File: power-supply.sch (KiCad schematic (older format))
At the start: 107 parts, among them IC1 TPS54561, J12 S2B-PH-K-S_LF__SN_, Q1 BSS138APW, Q2 BSS138APW, Q3 BSS138APW, Q4 BSS138APW, Q5 BSS138APW, Q6 BSS138APW, U10 TPS62823DLCT, U11 TPS62823DLCT, U12 TPS62823DLCT, U13 TPS62823DLCT, U16 TPS62823DLCT, U9 LM3881MME_NOPB

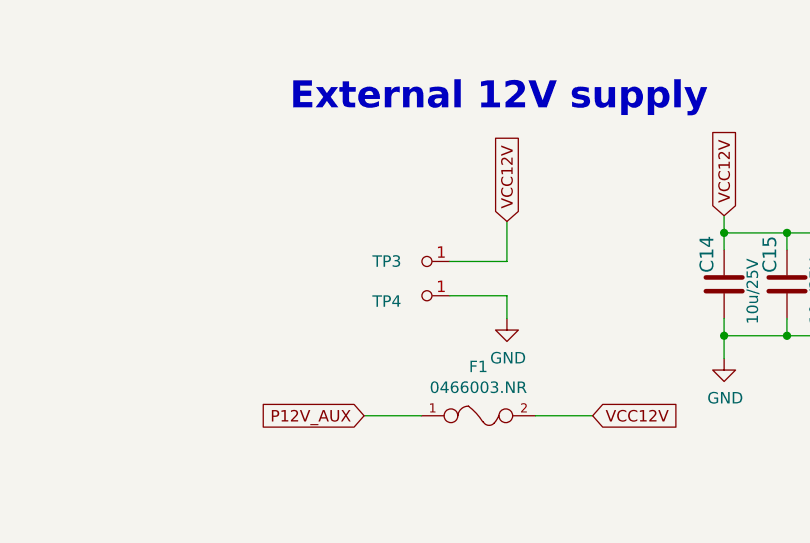
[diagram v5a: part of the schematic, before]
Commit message: Add aux pwr connector
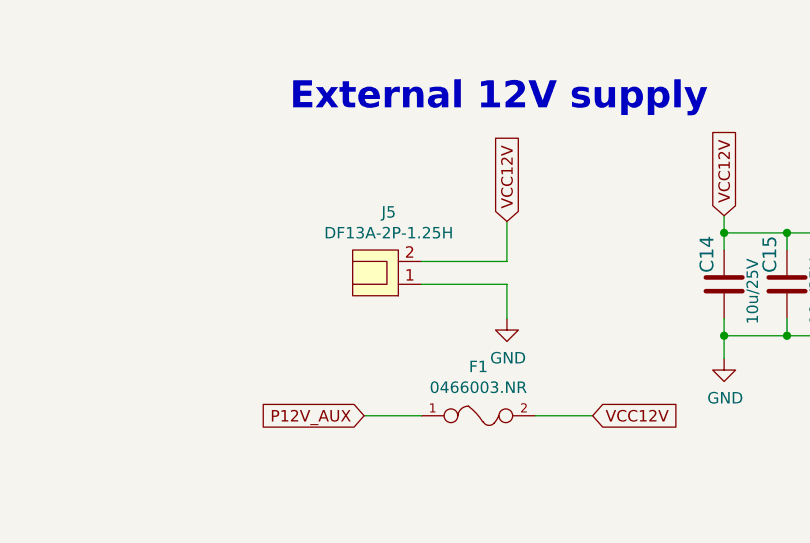
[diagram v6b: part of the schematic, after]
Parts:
- removed TP3, TP4: RCW-0C, artix-dc-scm-footprints:PROBE_PAD_1206, symbol artix-dc-scm:RCW-0C
- added J5: DF13A-2P-1.25H, artix-dc-scm-footprints:DF13A-2P-1.25H, symbol artix-dc-scm:DF13A-2P-1.25H
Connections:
- net GND: now also J5.1
- net VCC12V: now also J5.2
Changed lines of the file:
@@
-	0    1    1    0
-$EndComp
-$Comp
-L artix-dc-scm:RCW-0C TP3
-U 1 1 5FE83A9D
-P 1900 1575
-F 0 "TP3" V 1900 1400 50  0000 C CNN
-F 1 "RCW-0C" V 1766 1622 50  0001 C CNN
-F 2 "artix-dc-scm-footprints:PROBE_PAD_1206" H 2100 1775 60  0001 L CNN
-F 3 "https://www.te.com/commerce/DocumentDelivery/DDEController?Action=srchrtrv&DocNm=1773266&DocType=DS&DocLang=English" H 2100 1875 60  0001 L CNN
-F 4 "RCW-0C" H 2100 2075 60  0001 L CNN "MPN"
-F 5 "TE Connectivity AMP Connectors" H 2100 2675 60  0001 L CNN "Manufacturer"
-	1    1900 1575
-	0    1    1    0
-$EndComp
-$Comp
-L artix-dc-scm:RCW-0C TP4
-U 1 1 5FEA4BA8
-P 1900 1725
-F 0 "TP4" V 1925 1550 50  0000 C CNN
-F 1 "RCW-0C" V 1766 1772 50  0001 C CNN
-F 2 "artix-dc-scm-footprints:PROBE_PAD_1206" H 2100 1925 60  0001 L CNN
-F 3 "https://www.te.com/commerce/DocumentDelivery/DDEController?Action=srchrtrv&DocNm=1773266&DocType=DS&DocLang=English" H 2100 2025 60  0001 L CNN
-F 4 "RCW-0C" H 2100 2225 60  0001 L CNN "MPN"
-F 5 "TE Connectivity AMP Connectors" H 2100 2825 60  0001 L CNN "Manufacturer"
-	1    1900 1725
 	0    1    1    0
 $EndComp
 Text GLabel 2250 1400 1    50   Input ~ 0
 VCC12V
-Wire Wire Line
-	2000 1575 2250 1575
 Wire Wire Line
 	2250 1575 2250 1400
@@
 $EndComp
 Wire Wire Line
-	2000 1725 2250 1725
-Wire Wire Line
-	2250 1725 2250 1825
+	2250 1675 2250 1825
 Text GLabel 1625 2250 0    50   Input ~ 0
 P12V_AUX
@@
 Text Notes 8825 5925 0    50   ~ 0
 3v3 required by I3C translator
+$Comp
+L artix-dc-scm:DF13A-2P-1.25H J5
+U 1 1 601AA6B2
+P 1675 1525
+F 0 "J5" H 1617 1360 50  0000 C CNN
+F 1 "DF13A-2P-1.25H" H 1617 1451 50  0000 C CNN
+F 2 "artix-dc-scm-footprints:DF13A-2P-1.25H" H 1575 1075 50  0001 C CNN
+F 3 "" H 1675 1475 50  0001 C CNN
+F 4 "DF13A-2P-1.25H" H 1725 1275 50  0001 C CNN "MPN"
+F 5 "Hirose" H 1675 1175 50  0001 C CNN "Manufacturer"
+	1    1675 1525
+	-1   0    0    1
+$EndComp
+Wire Wire Line
+	1875 1575 2250 1575
+Wire Wire Line
+	1875 1675 2250 1675
 $EndSCHEMATC

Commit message: Fix USB3300 circuit
-remove 1V8 connection
-add capacitance at internal 1v8 regulators
-apply changes to PCB
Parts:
- C101, C103, C2, C75, C76, C77, C78, C83, C84, C85, C86, C87, C88, C89, C90: footprint artix-dc-scm-footprints:0402-cap -> _autosave-artix-dc-scm-footprints:0402-cap; symbol artix-dc-scm:C_10u_0402 -> _autosave-artix-dc-scm:C_10u_0402
- C14, C15, C16: footprint artix-dc-scm-footprints:0603-cap -> _autosave-artix-dc-scm-footprints:0603-cap; symbol artix-dc-scm:C_10u_25V_0603 -> _autosave-artix-dc-scm:C_10u_25V_0603
- C3, C79, C80, C81, C82: footprint artix-dc-scm-footprints:0402-res -> _autosave-artix-dc-scm-footprints:0402-res; symbol artix-dc-scm:C_120p_0402 -> _autosave-artix-dc-scm:C_120p_0402
- C64, C69: footprint artix-dc-scm-footprints:0402-cap -> _autosave-artix-dc-scm-footprints:0402-cap; symbol artix-dc-scm:C_10n_0402 -> _autosave-artix-dc-scm:C_10n_0402
- C65, C66, C67: footprint artix-dc-scm-footprints:0603-cap -> _autosave-artix-dc-scm-footprints:0603-cap; symbol artix-dc-scm:C_2u2_0603_25V -> _autosave-artix-dc-scm:C_2u2_0603_25V
- C68: footprint artix-dc-scm-footprints:0402-cap -> _autosave-artix-dc-scm-footprints:0402-cap; symbol artix-dc-scm:C_4n7_0402 -> _autosave-artix-dc-scm:C_4n7_0402
- C70: footprint artix-dc-scm-footprints:0402-cap -> _autosave-artix-dc-scm-footprints:0402-cap; symbol artix-dc-scm:C_47p_0402 -> _autosave-artix-dc-scm:C_47p_0402
- C71: footprint artix-dc-scm-footprints:0402-cap -> _autosave-artix-dc-scm-footprints:0402-cap; symbol artix-dc-scm:C_100n_0402-artix-dc-scm -> _autosave-artix-dc-scm:C_100n_0402-artix-dc-scm
- C72, C73, C74: footprint artix-dc-scm-footprints:0603-cap -> _autosave-artix-dc-scm-footprints:0603-cap; symbol artix-dc-scm:C_47u_0603 -> _autosave-artix-dc-scm:C_47u_0603
- D14, D4, D5, D6, D7, D8: footprint artix-dc-scm-footprints:LED_0603 -> _autosave-artix-dc-scm-footprints:LED_0603; symbol artix-dc-scm:LG_L29K-G2J1-24-Z -> _autosave-artix-dc-scm:LG_L29K-G2J1-24-Z
- D3: footprint artix-dc-scm-footprints:PDS760-13 -> _autosave-artix-dc-scm-footprints:PDS760-13; symbol artix-dc-scm:PDS760-13 -> _autosave-artix-dc-scm:PDS760-13
- F1: footprint artix-dc-scm-footprints:1206-Fuse-Littelfuse-0466-0-0-MFG -> _autosave-artix-dc-scm-footprints:1206-Fuse-Littelfuse-0466-0-0-MFG; symbol artix-dc-scm:0466003.NR -> _autosave-artix-dc-scm:0466003.NR
- IC1: footprint artix-dc-scm-footprints:WSON-10_4x4 -> _autosave-artix-dc-scm-footprints:WSON-10_4x4; symbol artix-dc-scm:TPS54561 -> _autosave-artix-dc-scm:TPS54561
- J12: footprint artix-dc-scm-footprints:PinHeader_1x2_P2mm_Drill1mm_RA -> _autosave-artix-dc-scm-footprints:PinHeader_1x2_P2mm_Drill1mm_RA; symbol artix-dc-scm:S2B-PH-K-S_LF__SN_ -> _autosave-artix-dc-scm:S2B-PH-K-S_LF__SN_
- J5: footprint artix-dc-scm-footprints:DF13A-2P-1.25H -> _autosave-artix-dc-scm-footprints:DF13A-2P-1.25H; symbol artix-dc-scm:DF13A-2P-1.25H -> _autosave-artix-dc-scm:DF13A-2P-1.25H
- L1: footprint artix-dc-scm-footprints:WE_7447798720 -> _autosave-artix-dc-scm-footprints:WE_7447798720; symbol artix-dc-scm:WE_7447798720 -> _autosave-artix-dc-scm:WE_7447798720
- L2, L3, L4, L5, L6: footprint artix-dc-scm-footprints:IHLP-1212AE -> _autosave-artix-dc-scm-footprints:IHLP-1212AE; symbol artix-dc-scm:IHLP1212AEERR47M11 -> _autosave-artix-dc-scm:IHLP1212AEERR47M11
- Q1, Q2, Q3, Q4, Q5, Q6: footprint artix-dc-scm-footprints:SC70-3 -> _autosave-artix-dc-scm-footprints:SC70-3; symbol artix-dc-scm:BSS138APW -> _autosave-artix-dc-scm:BSS138APW
- R138, R14, R15, R16, R185: footprint artix-dc-scm-footprints:0402-res -> _autosave-artix-dc-scm-footprints:0402-res; symbol artix-dc-scm:R_0R_0402 -> _autosave-artix-dc-scm:R_0R_0402
- R139, R140, R141, R142, R188: footprint artix-dc-scm-footprints:0603-res -> _autosave-artix-dc-scm-footprints:0603-res; symbol artix-dc-scm:R_0R_0603 -> _autosave-artix-dc-scm:R_0R_0603
- R186, R187, R68, R74, R76, R78, R80: footprint artix-dc-scm-footprints:0402-res -> _autosave-artix-dc-scm-footprints:0402-res; symbol artix-dc-scm:R_100k_0402 -> _autosave-artix-dc-scm:R_100k_0402
- R189, R61, R91, R92, R93: footprint artix-dc-scm-footprints:0402-res -> _autosave-artix-dc-scm-footprints:0402-res; symbol artix-dc-scm:R_10k_0402 -> _autosave-artix-dc-scm:R_10k_0402
- R190, R62, R63, R64, R65, R94, R95, R96, R97, R98: footprint artix-dc-scm-footprints:0402-res -> _autosave-artix-dc-scm-footprints:0402-res; symbol artix-dc-scm:R_1k_0402 -> _autosave-artix-dc-scm:R_1k_0402
- R66: footprint artix-dc-scm-footprints:0402-res -> _autosave-artix-dc-scm-footprints:0402-res; symbol artix-dc-scm:R_16k9_0402 -> _autosave-artix-dc-scm:R_16k9_0402
- R67: footprint artix-dc-scm-footprints:0402-res -> _autosave-artix-dc-scm-footprints:0402-res; symbol artix-dc-scm:R_243k_0402 -> _autosave-artix-dc-scm:R_243k_0402
- R69: footprint artix-dc-scm-footprints:1206-res -> _autosave-artix-dc-scm-footprints:1206-res; symbol artix-dc-scm:R_0R_1206 -> _autosave-artix-dc-scm:R_0R_1206
- R70: footprint artix-dc-scm-footprints:0402-res -> _autosave-artix-dc-scm-footprints:0402-res; symbol artix-dc-scm:R_49R9_0402 -> _autosave-artix-dc-scm:R_49R9_0402
- R71: footprint artix-dc-scm-footprints:0402-res -> _autosave-artix-dc-scm-footprints:0402-res; symbol artix-dc-scm:R_53k6_0402 -> _autosave-artix-dc-scm:R_53k6_0402
- R72: footprint artix-dc-scm-footprints:0402-res -> _autosave-artix-dc-scm-footprints:0402-res; symbol artix-dc-scm:R_10k2_0402 -> _autosave-artix-dc-scm:R_10k2_0402
- R73: footprint artix-dc-scm-footprints:0402-res -> _autosave-artix-dc-scm-footprints:0402-res; symbol artix-dc-scm:R_453k_0402 -> _autosave-artix-dc-scm:R_453k_0402
- R75: footprint artix-dc-scm-footprints:0402-res -> _autosave-artix-dc-scm-footprints:0402-res; symbol artix-dc-scm:R_200k_0402-artix-dc-scm -> _autosave-artix-dc-scm:R_200k_0402-artix-dc-scm
- R77: footprint artix-dc-scm-footprints:0402-res -> _autosave-artix-dc-scm-footprints:0402-res; symbol artix-dc-scm:R_66k5_0402 -> _autosave-artix-dc-scm:R_66k5_0402
- R79: footprint artix-dc-scm-footprints:0402-res -> _autosave-artix-dc-scm-footprints:0402-res; symbol artix-dc-scm:R_124k_0402 -> _autosave-artix-dc-scm:R_124k_0402
- TP1: footprint artix-dc-scm-footprints:Testpoint_smd_1mm -> _autosave-artix-dc-scm-footprints:Testpoint_smd_1mm; symbol artix-dc-scm:TP_SMD1MM -> _autosave-artix-dc-scm:TP_SMD1MM
- U10, U11, U12, U13, U16: footprint artix-dc-scm-footprints:QFN-8_2x1mm -> _autosave-artix-dc-scm-footprints:QFN-8_2x1mm; symbol artix-dc-scm:TPS62823DLCT -> _autosave-artix-dc-scm:TPS62823DLCT
- U9: footprint artix-dc-scm-footprints:VSSOP8-Texas_Instruments-DGK0008A -> _autosave-artix-dc-scm-footprints:VSSOP8-Texas_Instruments-DGK0008A; symbol artix-dc-scm:LM3881MME_NOPB -> _autosave-artix-dc-scm:LM3881MME_NOPB

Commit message: Fixed libs
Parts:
- C101, C103, C2, C75, C76, C77, C78, C83, C84, C85, C86, C87, C88, C89, C90: footprint _autosave-artix-dc-scm-footprints:0402-cap -> artix-dc-scm-footprints:0402-cap; symbol _autosave-artix-dc-scm:C_10u_0402 -> artix-dc-scm:C_10u_0402
- C14, C15, C16: footprint _autosave-artix-dc-scm-footprints:0603-cap -> artix-dc-scm-footprints:0603-cap; symbol _autosave-artix-dc-scm:C_10u_25V_0603 -> artix-dc-scm:C_10u_25V_0603
- C3, C79, C80, C81, C82: footprint _autosave-artix-dc-scm-footprints:0402-res -> artix-dc-scm-footprints:0402-res; symbol _autosave-artix-dc-scm:C_120p_0402 -> artix-dc-scm:C_120p_0402
- C64, C69: footprint _autosave-artix-dc-scm-footprints:0402-cap -> artix-dc-scm-footprints:0402-cap; symbol _autosave-artix-dc-scm:C_10n_0402 -> artix-dc-scm:C_10n_0402
- C65, C66, C67: footprint _autosave-artix-dc-scm-footprints:0603-cap -> artix-dc-scm-footprints:0603-cap; symbol _autosave-artix-dc-scm:C_2u2_0603_25V -> artix-dc-scm:C_2u2_0603_25V
- C68: footprint _autosave-artix-dc-scm-footprints:0402-cap -> artix-dc-scm-footprints:0402-cap; symbol _autosave-artix-dc-scm:C_4n7_0402 -> artix-dc-scm:C_4n7_0402
- C70: footprint _autosave-artix-dc-scm-footprints:0402-cap -> artix-dc-scm-footprints:0402-cap; symbol _autosave-artix-dc-scm:C_47p_0402 -> artix-dc-scm:C_47p_0402
- C71: footprint _autosave-artix-dc-scm-footprints:0402-cap -> artix-dc-scm-footprints:0402-cap; symbol _autosave-artix-dc-scm:C_100n_0402-artix-dc-scm -> artix-dc-scm:C_100n_0402-artix-dc-scm
- C72, C73, C74: footprint _autosave-artix-dc-scm-footprints:0603-cap -> artix-dc-scm-footprints:0603-cap; symbol _autosave-artix-dc-scm:C_47u_0603 -> artix-dc-scm:C_47u_0603
- D14, D4, D5, D6, D7, D8: footprint _autosave-artix-dc-scm-footprints:LED_0603 -> artix-dc-scm-footprints:LED_0603; symbol _autosave-artix-dc-scm:LG_L29K-G2J1-24-Z -> artix-dc-scm:LG_L29K-G2J1-24-Z
- D3: footprint _autosave-artix-dc-scm-footprints:PDS760-13 -> artix-dc-scm-footprints:PDS760-13; symbol _autosave-artix-dc-scm:PDS760-13 -> artix-dc-scm:PDS760-13
- F1: footprint _autosave-artix-dc-scm-footprints:1206-Fuse-Littelfuse-0466-0-0-MFG -> artix-dc-scm-footprints:1206-Fuse-Littelfuse-0466-0-0-MFG; symbol _autosave-artix-dc-scm:0466003.NR -> artix-dc-scm:0466003.NR
- IC1: footprint _autosave-artix-dc-scm-footprints:WSON-10_4x4 -> artix-dc-scm-footprints:WSON-10_4x4; symbol _autosave-artix-dc-scm:TPS54561 -> artix-dc-scm:TPS54561
- J12: footprint _autosave-artix-dc-scm-footprints:PinHeader_1x2_P2mm_Drill1mm_RA -> artix-dc-scm-footprints:PinHeader_1x2_P2mm_Drill1mm_RA; symbol _autosave-artix-dc-scm:S2B-PH-K-S_LF__SN_ -> artix-dc-scm:S2B-PH-K-S_LF__SN_
- J5: footprint _autosave-artix-dc-scm-footprints:DF13A-2P-1.25H -> artix-dc-scm-footprints:DF13A-2P-1.25H; symbol _autosave-artix-dc-scm:DF13A-2P-1.25H -> artix-dc-scm:DF13A-2P-1.25H
- L1: footprint _autosave-artix-dc-scm-footprints:WE_7447798720 -> artix-dc-scm-footprints:WE_7447798720; symbol _autosave-artix-dc-scm:WE_7447798720 -> artix-dc-scm:WE_7447798720
- L2, L3, L4, L5, L6: footprint _autosave-artix-dc-scm-footprints:IHLP-1212AE -> artix-dc-scm-footprints:IHLP-1212AE; symbol _autosave-artix-dc-scm:IHLP1212AEERR47M11 -> artix-dc-scm:IHLP1212AEERR47M11
- Q1, Q2, Q3, Q4, Q5, Q6: footprint _autosave-artix-dc-scm-footprints:SC70-3 -> artix-dc-scm-footprints:SC70-3; symbol _autosave-artix-dc-scm:BSS138APW -> artix-dc-scm:BSS138APW
- R138, R14, R15, R16, R185: footprint _autosave-artix-dc-scm-footprints:0402-res -> artix-dc-scm-footprints:0402-res; symbol _autosave-artix-dc-scm:R_0R_0402 -> artix-dc-scm:R_0R_0402
- R139, R140, R141, R142, R188: footprint _autosave-artix-dc-scm-footprints:0603-res -> artix-dc-scm-footprints:0603-res; symbol _autosave-artix-dc-scm:R_0R_0603 -> artix-dc-scm:R_0R_0603
- R186, R187, R68, R74, R76, R78, R80: footprint _autosave-artix-dc-scm-footprints:0402-res -> artix-dc-scm-footprints:0402-res; symbol _autosave-artix-dc-scm:R_100k_0402 -> artix-dc-scm:R_100k_0402
- R189, R61, R91, R92, R93: footprint _autosave-artix-dc-scm-footprints:0402-res -> artix-dc-scm-footprints:0402-res; symbol _autosave-artix-dc-scm:R_10k_0402 -> artix-dc-scm:R_10k_0402
- R190, R62, R63, R64, R65, R94, R95, R96, R97, R98: footprint _autosave-artix-dc-scm-footprints:0402-res -> artix-dc-scm-footprints:0402-res; symbol _autosave-artix-dc-scm:R_1k_0402 -> artix-dc-scm:R_1k_0402
- R66: footprint _autosave-artix-dc-scm-footprints:0402-res -> artix-dc-scm-footprints:0402-res; symbol _autosave-artix-dc-scm:R_16k9_0402 -> artix-dc-scm:R_16k9_0402
- R67: footprint _autosave-artix-dc-scm-footprints:0402-res -> artix-dc-scm-footprints:0402-res; symbol _autosave-artix-dc-scm:R_243k_0402 -> artix-dc-scm:R_243k_0402
- R69: footprint _autosave-artix-dc-scm-footprints:1206-res -> artix-dc-scm-footprints:1206-res; symbol _autosave-artix-dc-scm:R_0R_1206 -> artix-dc-scm:R_0R_1206
- R70: footprint _autosave-artix-dc-scm-footprints:0402-res -> artix-dc-scm-footprints:0402-res; symbol _autosave-artix-dc-scm:R_49R9_0402 -> artix-dc-scm:R_49R9_0402
- R71: footprint _autosave-artix-dc-scm-footprints:0402-res -> artix-dc-scm-footprints:0402-res; symbol _autosave-artix-dc-scm:R_53k6_0402 -> artix-dc-scm:R_53k6_0402
- R72: footprint _autosave-artix-dc-scm-footprints:0402-res -> artix-dc-scm-footprints:0402-res; symbol _autosave-artix-dc-scm:R_10k2_0402 -> artix-dc-scm:R_10k2_0402
- R73: footprint _autosave-artix-dc-scm-footprints:0402-res -> artix-dc-scm-footprints:0402-res; symbol _autosave-artix-dc-scm:R_453k_0402 -> artix-dc-scm:R_453k_0402
- R75: footprint _autosave-artix-dc-scm-footprints:0402-res -> artix-dc-scm-footprints:0402-res; symbol _autosave-artix-dc-scm:R_200k_0402-artix-dc-scm -> artix-dc-scm:R_200k_0402-artix-dc-scm
- R77: footprint _autosave-artix-dc-scm-footprints:0402-res -> artix-dc-scm-footprints:0402-res; symbol _autosave-artix-dc-scm:R_66k5_0402 -> artix-dc-scm:R_66k5_0402
- R79: footprint _autosave-artix-dc-scm-footprints:0402-res -> artix-dc-scm-footprints:0402-res; symbol _autosave-artix-dc-scm:R_124k_0402 -> artix-dc-scm:R_124k_0402
- TP1: footprint _autosave-artix-dc-scm-footprints:Testpoint_smd_1mm -> artix-dc-scm-footprints:Testpoint_smd_1mm; symbol _autosave-artix-dc-scm:TP_SMD1MM -> artix-dc-scm:TP_SMD1MM
- U10, U11, U12, U13, U16: footprint _autosave-artix-dc-scm-footprints:QFN-8_2x1mm -> artix-dc-scm-footprints:QFN-8_2x1mm; symbol _autosave-artix-dc-scm:TPS62823DLCT -> artix-dc-scm:TPS62823DLCT
- U9: footprint _autosave-artix-dc-scm-footprints:VSSOP8-Texas_Instruments-DGK0008A -> artix-dc-scm-footprints:VSSOP8-Texas_Instruments-DGK0008A; symbol _autosave-artix-dc-scm:LM3881MME_NOPB -> artix-dc-scm:LM3881MME_NOPB
